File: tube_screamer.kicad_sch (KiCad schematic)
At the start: 59 parts, among them Q1 MMBT5551, Q2 MMBT5551, Q3 MMBT5551, U1 NE5532

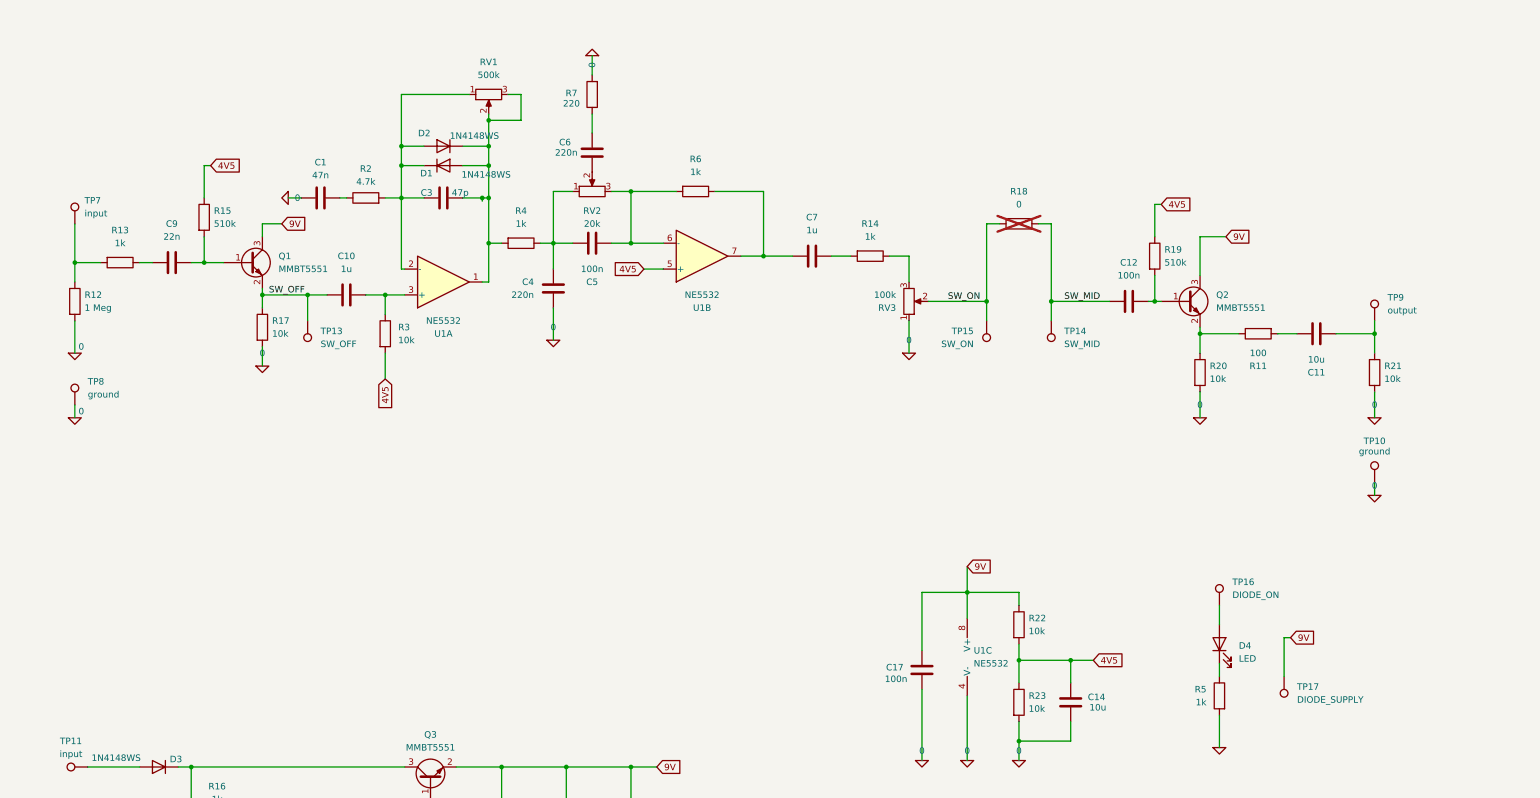
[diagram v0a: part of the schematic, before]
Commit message: Added connectors and switch.
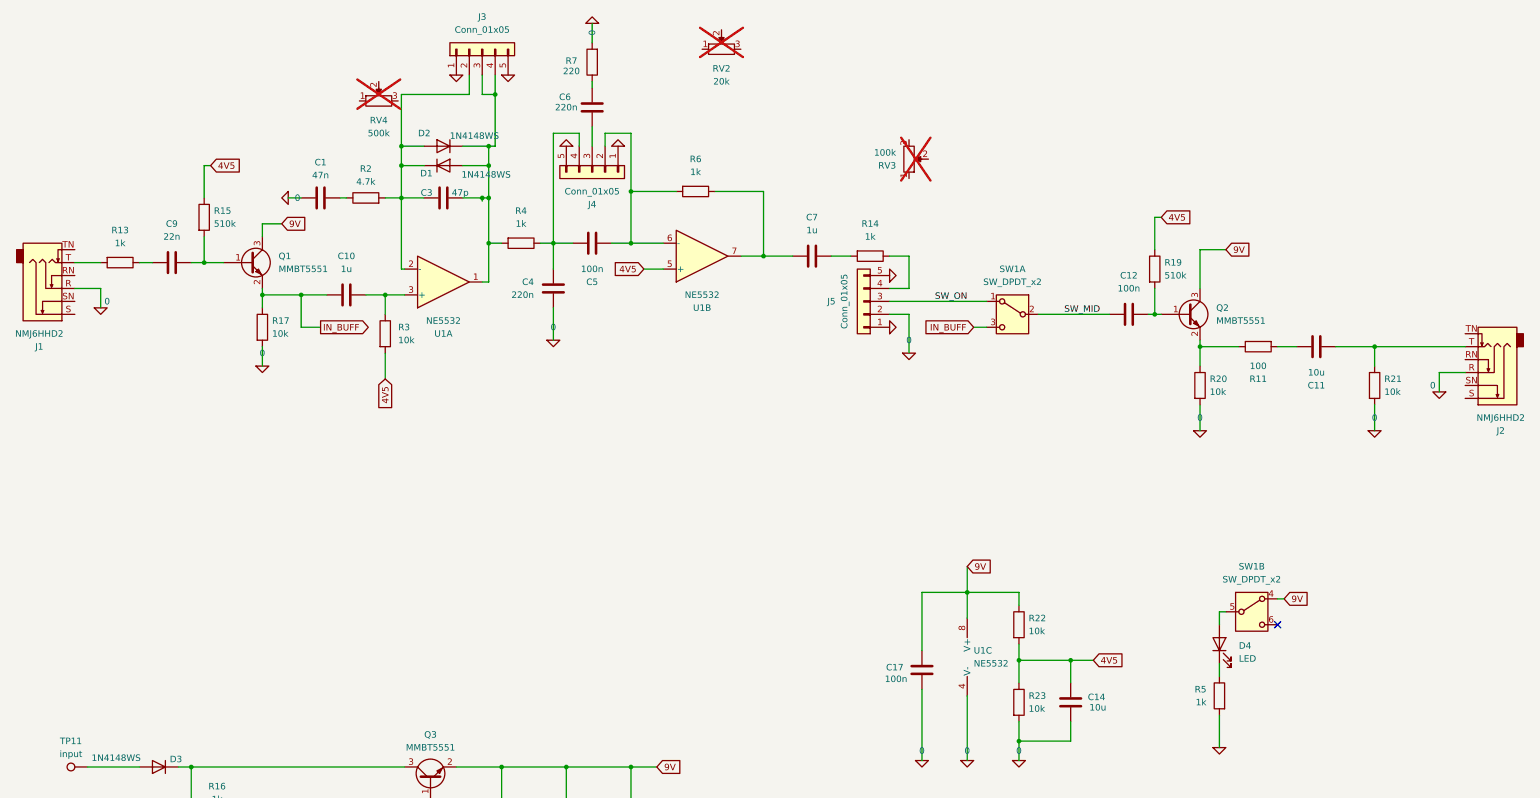
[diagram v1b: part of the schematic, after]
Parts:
- removed R12: 1 Meg, Resistor_SMD:R_0603_1608Metric_Pad0.98x0.95mm_HandSolder, symbol Device:R
- removed R18: 0, Resistor_SMD:R_0603_1608Metric_Pad0.98x0.95mm_HandSolder, symbol Device:R
- removed RV1: 500k, Potentiometer_THT:Potentiometer_Alpha_RD901F-40-00D_Single_Vertical, symbol Device:R_Potentiometer
- removed TP10, TP8: ground, TestPoint:TestPoint_THTPad_2.5x2.5mm_Drill1.2mm, symbol Connector:TestPoint
- removed TP13: SW_OFF, TestPoint:TestPoint_THTPad_2.5x2.5mm_Drill1.2mm, symbol Connector:TestPoint
- removed TP14: SW_MID, TestPoint:TestPoint_THTPad_2.5x2.5mm_Drill1.2mm, symbol Connector:TestPoint
- removed TP15: SW_ON, TestPoint:TestPoint_THTPad_2.5x2.5mm_Drill1.2mm, symbol Connector:TestPoint
- removed TP16: DIODE_ON, TestPoint:TestPoint_THTPad_2.5x2.5mm_Drill1.2mm, symbol Connector:TestPoint
- removed TP17: DIODE_SUPPLY, TestPoint:TestPoint_THTPad_2.5x2.5mm_Drill1.2mm, symbol Connector:TestPoint
- removed TP7: input, TestPoint:TestPoint_THTPad_2.5x2.5mm_Drill1.2mm, symbol Connector:TestPoint
- removed TP9: output, TestPoint:TestPoint_THTPad_2.5x2.5mm_Drill1.2mm, symbol Connector:TestPoint
- added J1, J2: NMJ6HHD2, Connector_Audio:Jack_6.35mm_Neutrik_NMJ6HHD2_Horizontal, symbol Connector_Audio:NMJ6HHD2
- added J3, J4, J5: Conn_01x05, Connector_JST:JST_EH_B5B-EH-A_1x05_P2.50mm_Vertical, symbol Connector_Generic:Conn_01x05
- added RV4: 500k, Potentiometer_THT:Potentiometer_Alpha_RD901F-40-00D_Single_Vertical, symbol Device:R_Potentiometer
- added SW1: SW_DPDT_x2, switch:switch_DPDT, symbol Switch:SW_DPDT_x2
- RV2, RV3: now not fitted
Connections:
- net 0: now also J1.R, J2.R, J3.1 (Pin_1), J3.5 (Pin_5), J4.1 (Pin_1), J4.5 (Pin_5), J5.1 (Pin_1), J5.2 (Pin_2), J5.5 (Pin_5); no longer RV3.1
- net 9V: now also SW1.4 (A)
- net SW_MID: now also SW1.2 (B)
- net SW_ON: now also J5.3 (Pin_3), SW1.1 (A); no longer RV3.2
- net at C3.1, D1.1 (K), D2.2 (A)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: now also J3.2 (Pin_2)
- net at C3.2, D1.2 (A), D2.1 (K)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: now also J3.3 (Pin_3), J3.4 (Pin_4)
- net at C4.2, C5.1, R4.1: now also J4.4 (Pin_4); no longer RV2.1
- net at C5.2, R6.2, U1.6 (-): now also J4.2 (Pin_2); no longer RV2.3
- net at RV3.3: no longer R14.1
- net at C11.2, R21.1: now also J2.T
- net at RV2.2: no longer C6.1
- net at R13.2: now also J1.T
- net at D4.2 (A): now also SW1.5 (B)
- net SW_OFF renamed IN_BUFF
- net IN_BUFF: now also SW1.3 (C)
- new net: J5.4 (Pin_4), R14.1
- new net: C6.1, J4.3 (Pin_3)
- no-connect marks 0 -> 1
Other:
- moved on the sheet: C11, C12, C6, Q2, R11, R19, R20, R21, R7

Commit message: Goin well.
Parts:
- removed TP11: input, TestPoint:TestPoint_THTPad_2.5x2.5mm_Drill1.2mm, symbol Connector:TestPoint
- removed TP12: ground, TestPoint:TestPoint_THTPad_2.5x2.5mm_Drill1.2mm, symbol Connector:TestPoint
- added BT1: Battery_Cell, pedale:BatteryHolder_Eagle_12BH611-GR, symbol Device:Battery_Cell
- added D5: 1N4148WS, Diode_SMD:D_SOD-323, symbol Diode:1N4148WS
- added D8: floating_green_led, pedale:floating_green_led, symbol pedale:floating_green_led
- added D9: floating_red_led, pedale:floating_red_led, symbol pedale:floating_red_led
- added H1, H2, H3, H4, H5: MountingHole, pedale:M3_hole_with_spacer, symbol Mechanical:MountingHole
- added J6: Barrel_Jack_MountingPin, Connector_BarrelJack:BarrelJack_GCT_DCJ200-10-A_Horizontal, symbol Connector:Barrel_Jack_MountingPin
- added P1: tube_screamer_front_panel, pedale:tube_screamer_front_plate, symbol pedale:tube_screamer_front_panel
- added RV1, RV7, RV9: floating_pot_knob, pedale:floating_pot_knob, symbol pedale:floating_pot_knob
- added RV5, RV6, RV8: floating_pot, pedale:floating_pot, symbol pedale:floating_pot
- added SIM1: Logo_Open_Hardware_Small, Symbol:OSHW-Logo2_7.3x6mm_SilkScreen, symbol Graphic:Logo_Open_Hardware_Small
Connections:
- net 0: now also BT1.2 (-), J6.2
- net at D3.1 (K), Q3.3 (C), R16.2: now also D5.1 (K)
- net at D3.2 (A): now also J6.1
- new net: BT1.1 (+), D5.2 (A)
- no-connect marks 1 -> 2

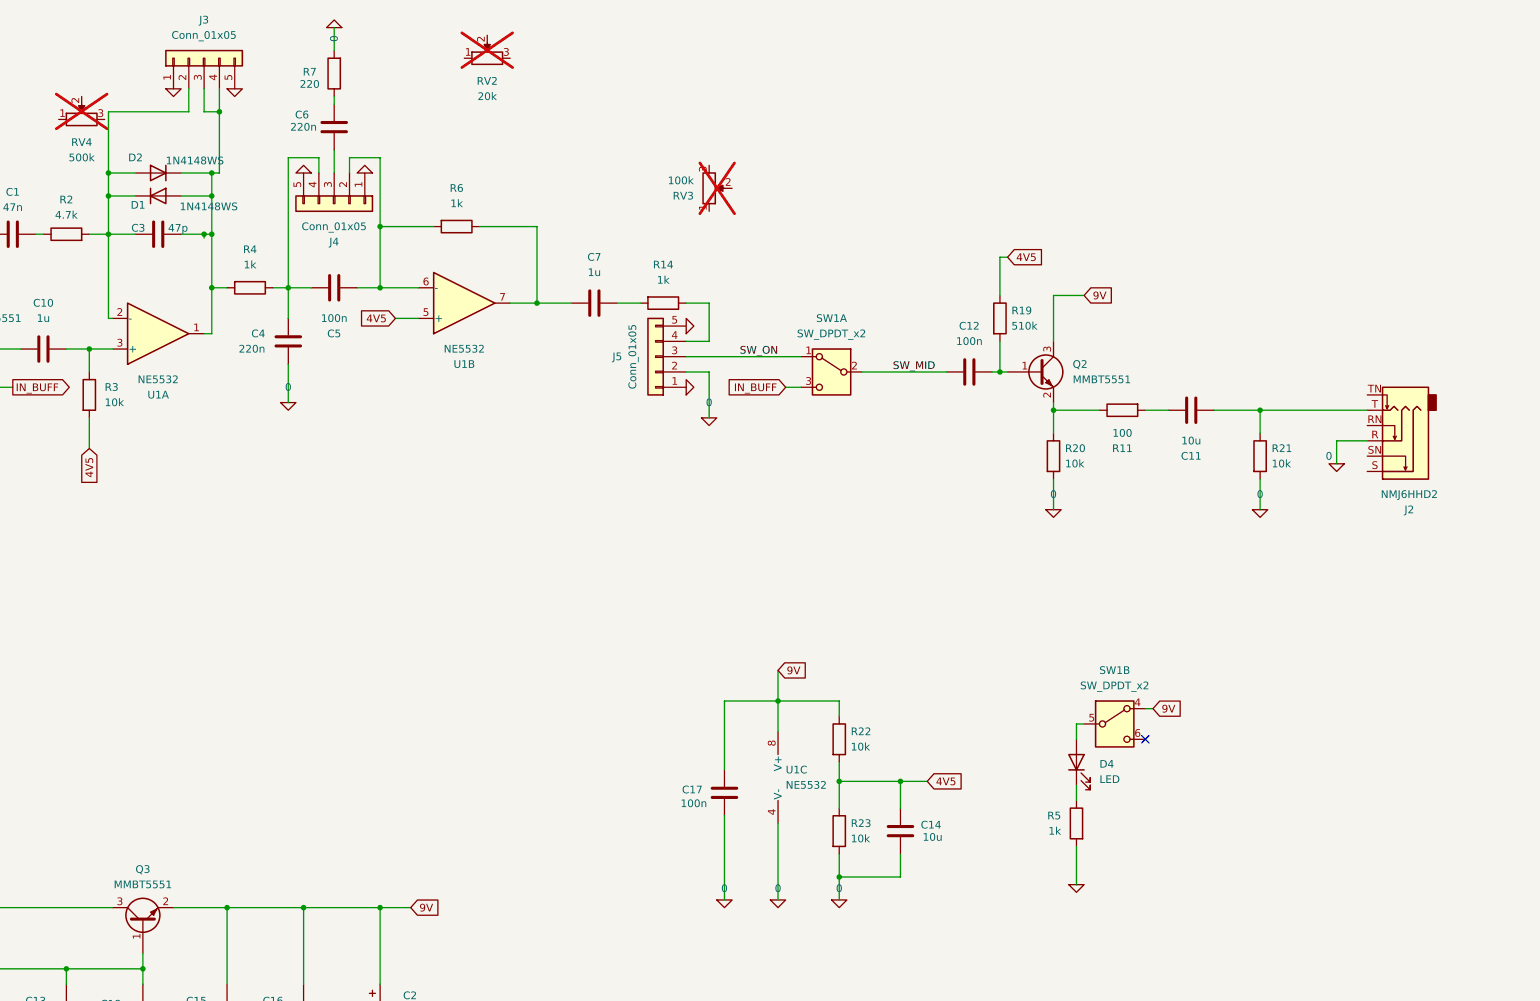
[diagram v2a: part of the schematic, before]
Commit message: 3D bodies
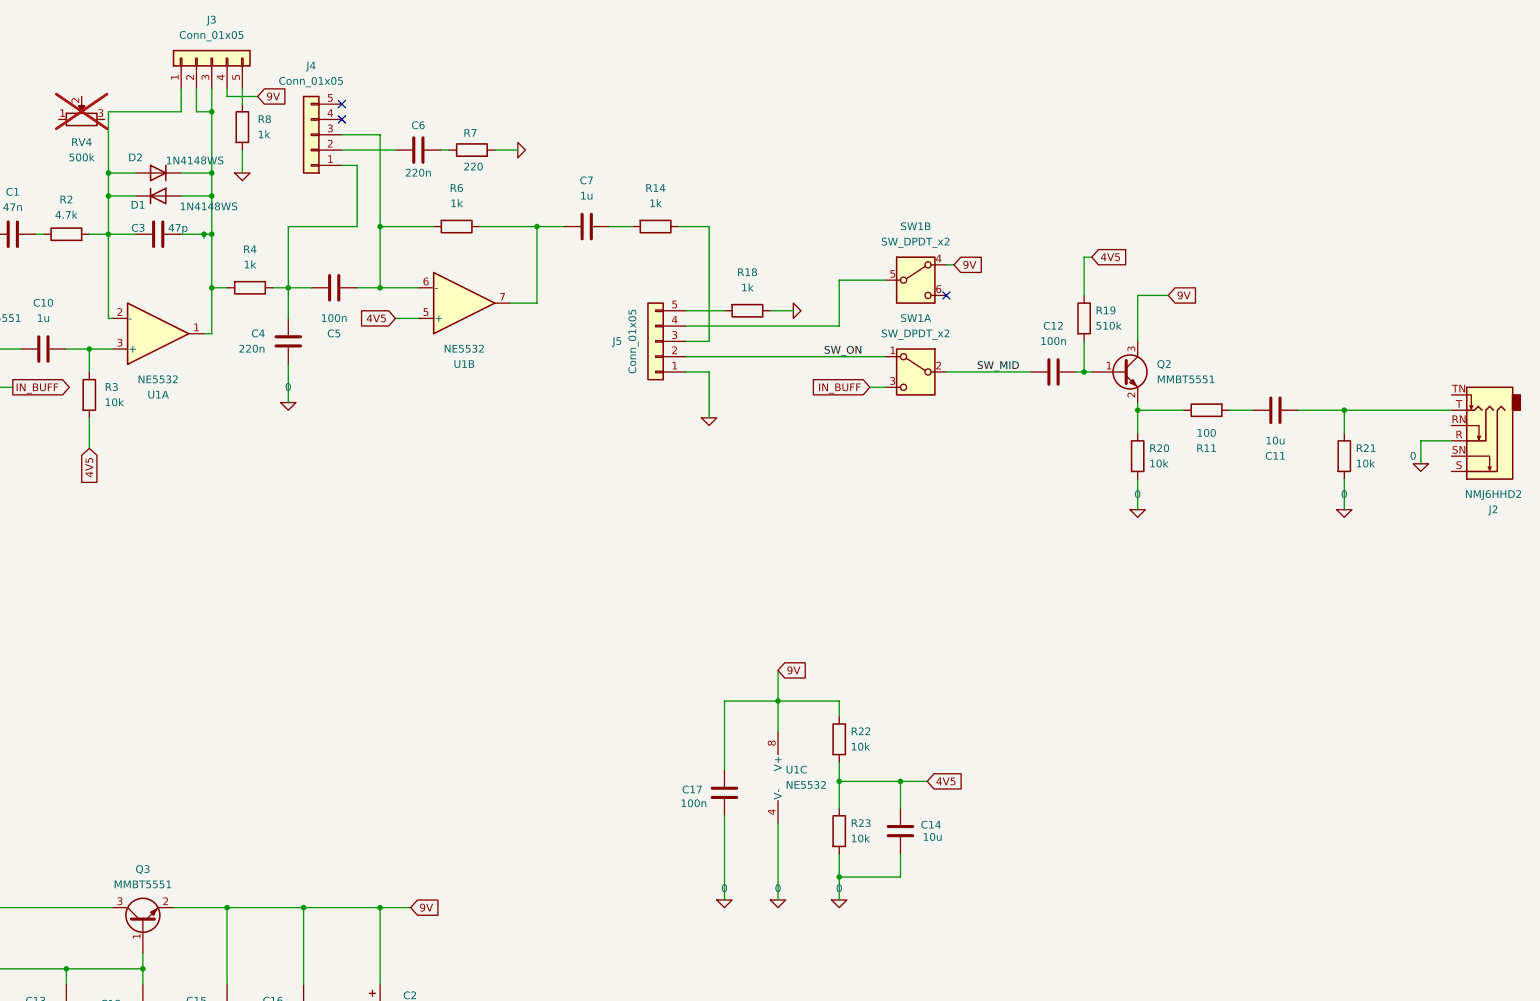
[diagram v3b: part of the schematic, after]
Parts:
- removed D4: LED, LED_THT:LED_D5.0mm, symbol Device:LED
- removed R5: 1k, Resistor_SMD:R_0603_1608Metric_Pad0.98x0.95mm_HandSolder, symbol Device:R
- removed RV2: 20k, Potentiometer_THT:Potentiometer_Alpha_RD901F-40-00D_Single_Vertical, symbol Device:R_Potentiometer
- removed RV3: 100k, Potentiometer_THT:Potentiometer_Alpha_RD901F-40-00D_Single_Vertical, symbol Device:R_Potentiometer
- added R18, R8: 1k, Resistor_SMD:R_0603_1608Metric_Pad0.98x0.95mm_HandSolder, symbol Device:R
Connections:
- net 0: now also R18.1, R8.2; no longer J3.1 (Pin_1), J3.5 (Pin_5), J4.1 (Pin_1), J4.5 (Pin_5), J5.2 (Pin_2), J5.5 (Pin_5)
- net 9V: now also J3.4 (Pin_4)
- net SW_ON: now also J5.2 (Pin_2); no longer J5.3 (Pin_3)
- net at C3.1, D1.1 (K), D2.2 (A)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: now also J3.1 (Pin_1); no longer J3.2 (Pin_2)
- net at C3.2, D1.2 (A), D2.1 (K)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: now also J3.2 (Pin_2); no longer J3.4 (Pin_4)
- net at C4.2, C5.1, R4.1: now also J4.1 (Pin_1); no longer J4.4 (Pin_4)
- net at C5.2, R6.2, U1.6 (-): now also J4.3 (Pin_3); no longer J4.2 (Pin_2)
- net at R14.1: now also J5.3 (Pin_3); no longer J5.4 (Pin_4)
- net at C6.1: now also J4.2 (Pin_2); no longer J4.3 (Pin_3)
- net at SW1.5 (B): now also J5.4 (Pin_4)
- new net: J3.5 (Pin_5), R8.1
- new net: J5.5 (Pin_5), R18.2
- no-connect marks 2 -> 4
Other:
- moved on the sheet: C11, C12, C6, C7, J2, J3, J4, J5, Q2, R11, R14, R19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

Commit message: Schematic cleaned.
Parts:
- removed RV4: 500k, Potentiometer_THT:Potentiometer_Alpha_RD901F-40-00D_Single_Vertical, symbol Device:R_Potentiometer
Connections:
- net OP_OUT: now reaches J5.3 (Pin_3), R14.1
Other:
- note added: "Clipping and tone stage"
- note added: "Input gain stage"
- note added: "Mounting and estetics"
- note added: "Output gain stage and selection switch"
- note added: "Power supply"
- moved on the sheet: BT1, C1, C10, C11, C12, C13, C14, C15, C16, C17, C18, C2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

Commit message: Schem fix
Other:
- note added: "Input buffer"
- note added: "Output buffer and selection switch"
- note removed: "Input gain stage"
- note removed: "Output gain stage and selection switch"
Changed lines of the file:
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@@
 		)
 	)
-	(text "Input gain stage"
+	(text "Input buffer"
 		(exclude_from_sim no)
 		(at 29.21 15.24 0)
@@
 		)
 	)
-	(text "Output gain stage and selection switch"
+	(text "Output buffer and selection switch"
 		(exclude_from_sim no)
 		(at 148.59 83.566 0)

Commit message: v1.
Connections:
- net 0: now also J1.S, J2.S
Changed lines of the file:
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@@
 	)
 	(junction
+		(at 41.91 57.15)
+		(diameter 0)
+		(color 0 0 0 0)
+	)
+	(junction
 		(at 205.74 121.92)
 		(diameter 0)
@@
 	)
 	(junction
+		(at 254 132.08)
+		(diameter 0)
+		(color 0 0 0 0)
+	)
+	(junction
 		(at 160.02 38.1)
 		(diameter 0)
@@
 	(wire
 		(pts
+			(xy 36.83 57.15) (xy 41.91 57.15)
+		)
+		(stroke
+			(width 0)
+			(type default)
+		)
+	)
+	(wire
+		(pts
 			(xy 269.24 33.655) (xy 269.24 38.1)
 		)
@@
 	(wire
 		(pts
-			(xy 41.91 52.07) (xy 41.91 55.88)
-		)
-		(stroke
-			(width 0)
-			(type default)
-		)
-	)
-	(wire
-		(pts
 			(xy 138.43 163.83) (xy 125.73 163.83)
 		)
@@
 	(wire
 		(pts
-			(xy 257.81 127) (xy 252.73 127)
+			(xy 257.81 127) (xy 254 127)
 		)
 		(stroke
@@
 	(wire
 		(pts
+			(xy 41.91 57.15) (xy 41.91 60.96)
+		)
+		(stroke
+			(width 0)
+			(type default)
+		)
+	)
+	(wire
+		(pts
 			(xy 248.92 20.32) (xy 259.08 20.32)
 		)
@@
 	(wire
 		(pts
+			(xy 41.91 52.07) (xy 41.91 57.15)
+		)
+		(stroke
+			(width 0)
+			(type default)
+		)
+	)
+	(wire
+		(pts
 			(xy 207.01 34.29) (xy 210.82 34.29)
 		)
@@
 	(wire
 		(pts
-			(xy 252.73 127) (xy 252.73 130.81)
+			(xy 254 127) (xy 254 132.08)
 		)
 		(stroke
@@
 	(wire
 		(pts
+			(xy 254 132.08) (xy 254 135.89)
+		)
+		(stroke
+			(width 0)
+			(type default)
+		)
+	)
+	(wire
+		(pts
 			(xy 143.51 62.23) (xy 142.875 62.23)
 		)
@@
 	(wire
 		(pts
+			(xy 254 132.08) (xy 257.81 132.08)
+		)
+		(stroke
+			(width 0)
+			(type default)
+		)
+	)
+	(wire
+		(pts
 			(xy 144.78 105.41) (xy 148.59 105.41)
 		)
@@
 	(symbol
 		(lib_id "Simulation_SPICE:0")
-		(at 41.91 55.88 0)
+		(at 41.91 60.96 0)
 		(unit 1)
 		(exclude_from_sim no)
@@
 		(dnp no)
 		(property "Reference" "#GND025"
-			(at 41.91 58.42 0)
+			(at 41.91 63.5 0)
 			(effects
 				(font
@@
 		)
 		(property "Value" "0"
-			(at 43.18 54.61 0)
+			(at 43.18 59.69 0)
 			(effects
 				(font
@@
 		)
 		(property "Footprint" ""
-			(at 41.91 55.88 0)
+			(at 41.91 60.96 0)
 			(effects
 				(font
@@
 		)
 		(property "Datasheet" "~"
-			(at 41.91 55.88 0)
+			(at 41.91 60.96 0)
 			(effects
 				(font
@@
 		)
 		(property "Description" ""
-			(at 41.91 55.88 0)
+			(at 41.91 60.96 0)
 			(effects
 				(font
@@
 	(symbol
 		(lib_id "Simulation_SPICE:0")
-		(at 252.73 130.81 0)
+		(at 254 135.89 0)
 		(mirror y)
 		(unit 1)
@@
 		(dnp no)
 		(property "Reference" "#GND026"
-			(at 252.73 133.35 0)
+			(at 254 138.43 0)
 			(effects
 				(font
@@
 		)
 		(property "Value" "0"
-			(at 251.46 129.54 0)
+			(at 252.73 134.62 0)
 			(effects
 				(font
@@
 		)
 		(property "Footprint" ""
-			(at 252.73 130.81 0)
+			(at 254 135.89 0)
 			(effects
 				(font
@@
 		)
 		(property "Datasheet" "~"
-			(at 252.73 130.81 0)
+			(at 254 135.89 0)
 			(effects
 				(font
@@
 		)
 		(property "Description" ""
-			(at 252.73 130.81 0)
+			(at 254 135.89 0)
 			(effects
 				(font

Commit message: Schematic fix, PCB final
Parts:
- removed C5: 100n, Capacitor_SMD:C_0603_1608Metric_Pad1.08x0.95mm_HandSolder, symbol Device:C
- added R25: 10k, Resistor_SMD:R_0603_1608Metric_Pad0.98x0.95mm_HandSolder, symbol Device:R
- added R47: 47k, Resistor_SMD:R_0603_1608Metric_Pad0.98x0.95mm_HandSolder, symbol Device:R
- added R48: 100, Resistor_SMD:R_0603_1608Metric_Pad0.98x0.95mm_HandSolder, symbol Device:R
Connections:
- net 4V5: now also R25.2; no longer U1.5 (+)
- net IN_BUFF: now also R48.1; no longer C10.1
- net at C3.1, D1.1 (K), D2.2 (A)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: now also R47.1; no longer J3.1 (Pin_1)
- net at C4.2, J4.1 (Pin_1), R4.1: now also U1.5 (+), R25.1
- new net: J3.1 (Pin_1), R47.2
- new net: C10.1, R48.2
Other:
- moved on the sheet: C10

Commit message: All errors removed
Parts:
- removed J1, J2: NMJ6HHD2, Connector_Audio:Jack_6.35mm_Neutrik_NMJ6HHD2_Horizontal, symbol Connector_Audio:NMJ6HHD2
- removed J6: Barrel_Jack_MountingPin, Connector_BarrelJack:BarrelJack_GCT_DCJ200-10-A_Horizontal, symbol Connector:Barrel_Jack_MountingPin
- removed RV1, RV7, RV9: floating_pot_knob, pedale:floating_pot_knob, symbol pedale:floating_pot_knob
- removed SW1: SW_DPDT_x2, switch:switch_DPDT, symbol Switch:SW_DPDT_x2
- added J1, J2: Jack_6.35, pedale:Jack_6.35mm, symbol pedale:Jack_6.35
- added J6: Barrel_Jack_Switch, pedale:BarrelJack, symbol Connector:Barrel_Jack_Switch
- added J7, J8: Conn_01x01_Socket, TestPoint:TestPoint_THTPad_D2.5mm_Drill1.2mm, symbol Connector:Conn_01x01_Socket
- added SW1: pedala_switch, pedale:foot_switch_tht_and_floating, symbol pedale:pedala_switch
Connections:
- net 0: now also J1.R, J1.S, J2.R, J2.S, J6.2; no longer BT1.2 (-)
- net 9V: now also SW1.4 (A)
- net IN_BUFF: now also SW1.3 (C)
- net SW_MID: now also SW1.2 (B)
- net SW_ON: now also SW1.1 (A)
- net at BT1.1 (+), D5.2 (A): now also J7.1 (Pin_1)
- net at C11.2, R21.1: now also J2.T
- net at R13.2: now also J1.T
- net at D3.2 (A): now also J6.1
- net at J5.4 (Pin_4): now also SW1.5 (B)
- new net: BT1.2 (-), J6.3, J8.1 (Pin_1)
- no-connect marks 4 -> 3
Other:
- moved on the sheet: D8
